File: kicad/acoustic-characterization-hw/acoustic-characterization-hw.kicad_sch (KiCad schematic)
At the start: 0 parts

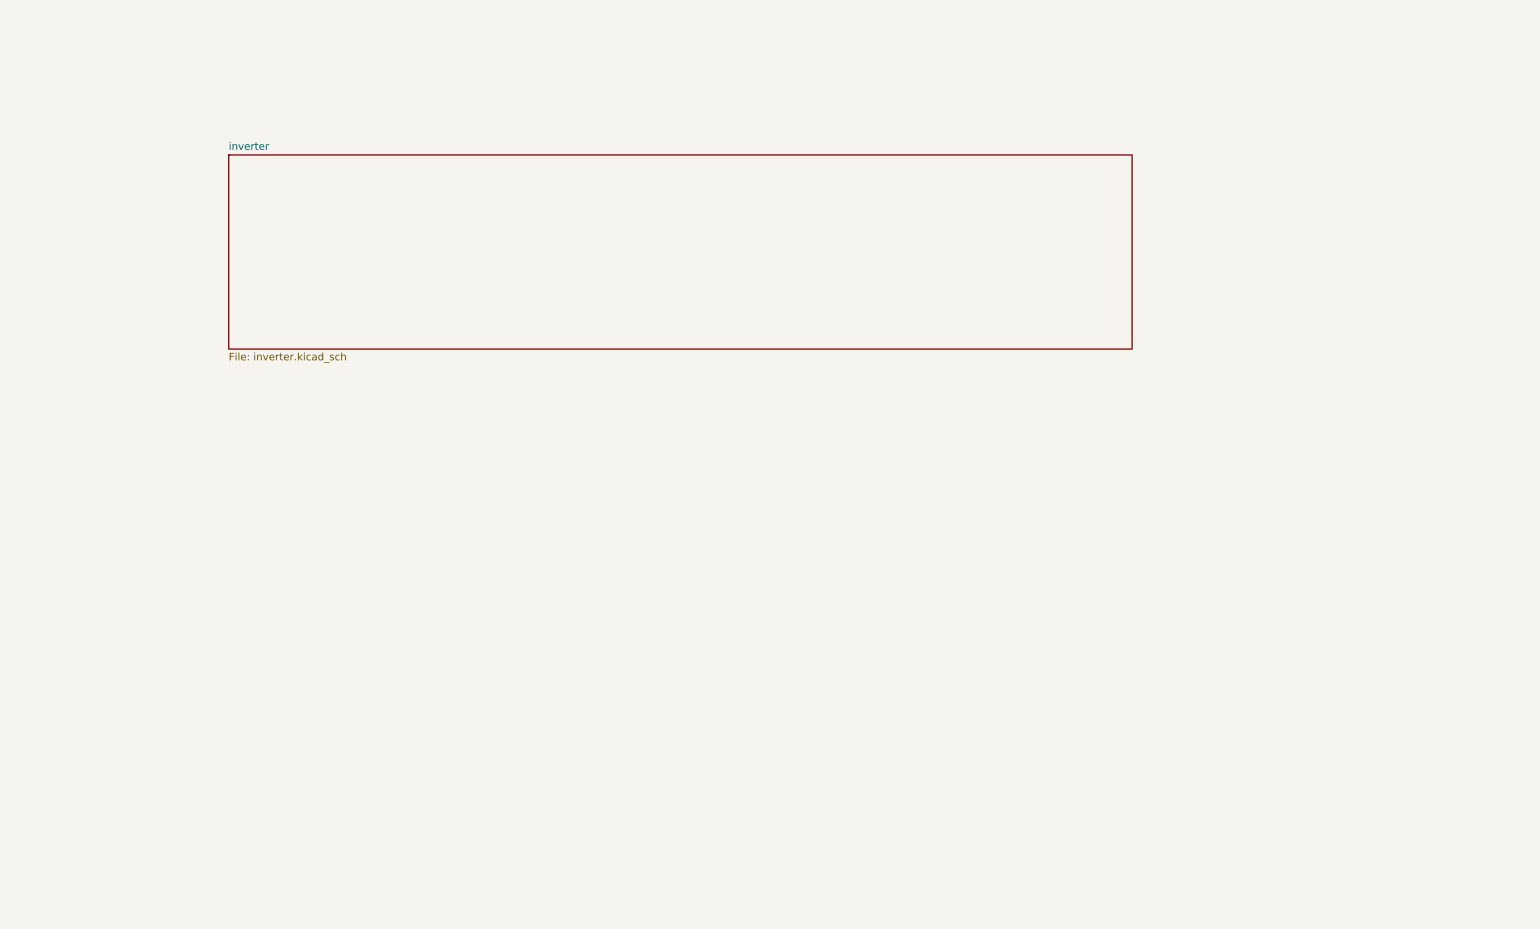
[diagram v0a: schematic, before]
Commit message: [kicad] Added analog front-end schematic and MS9280 symbol
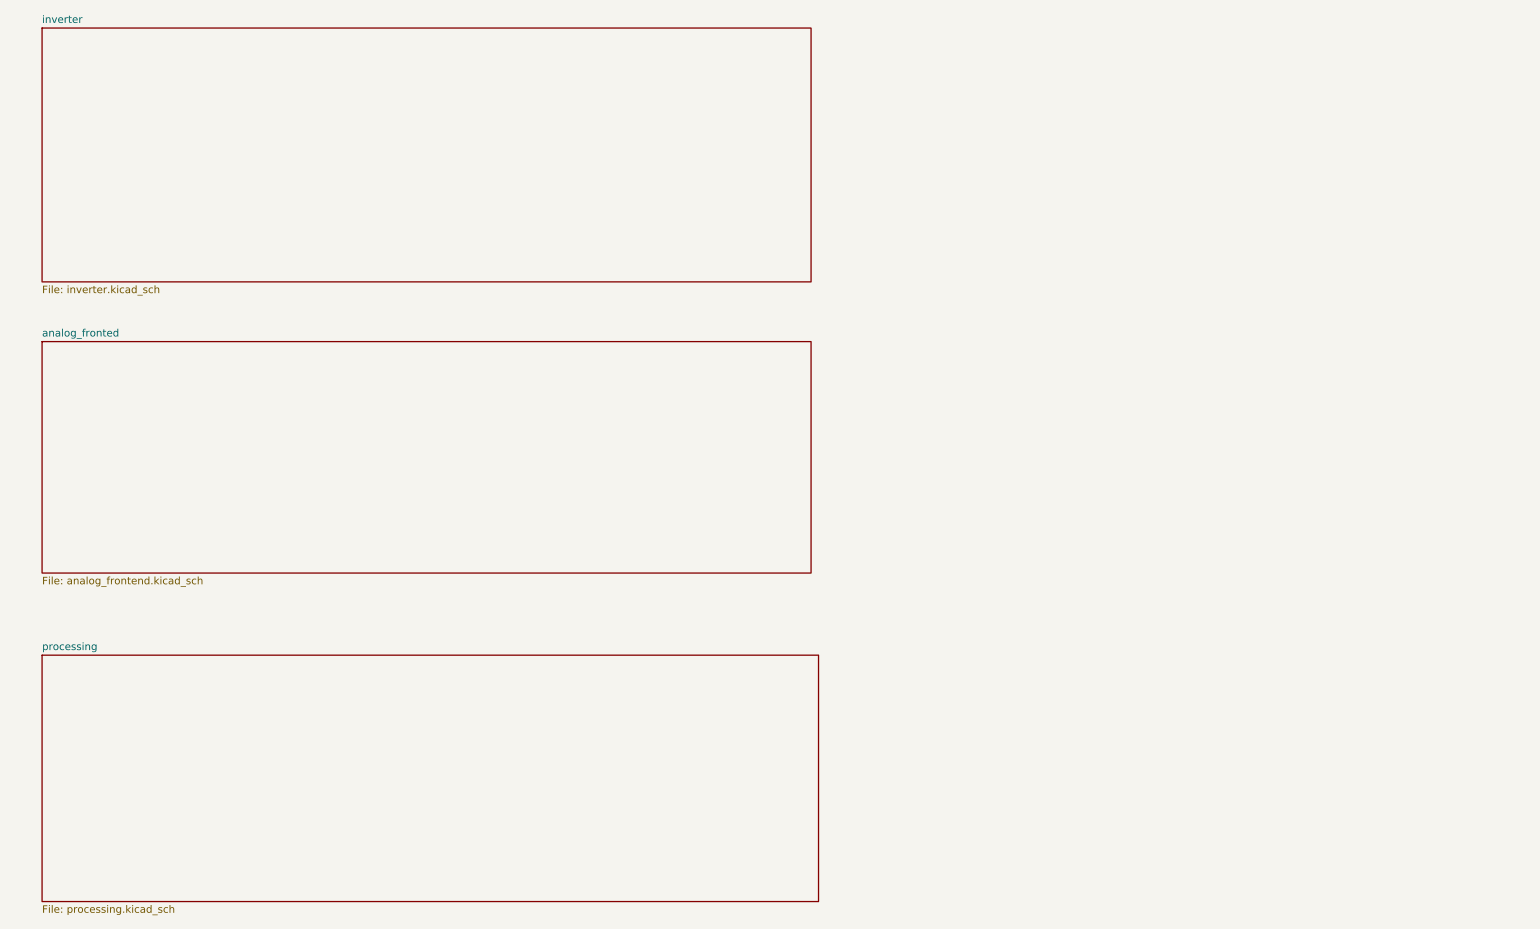
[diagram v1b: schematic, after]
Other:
- added sheet analog_fronted (analog_frontend.kicad_sch)
- added sheet processing (processing.kicad_sch)
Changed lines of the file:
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@@
 	(paper "A4")
 	(sheet
-		(at 52.07 43.18)
-		(size 153.67 33.02)
+		(at 20.32 74.93)
+		(size 130.81 39.37)
+		(fields_autoplaced yes)
+		(stroke
+			(width 0.1524)
+			(type solid)
+		)
+		(fill
+			(color 0 0 0 0.0000)
+		)
+		(property "Sheetname" "analog_fronted"
+			(at 20.32 74.2184 0)
+			(effects
+				(font
+					(size 1.27 1.27)
+				)
+				(justify left bottom)
+			)
+		)
+		(property "Sheetfile" "analog_frontend.kicad_sch"
+			(at 20.32 114.8846 0)
+			(effects
+				(font
+					(size 1.27 1.27)
+				)
+				(justify left top)
+			)
+		)
+		(instances
+			(project "acoustic-characterization-hw"
+				(path "/25b015c9-ab13-4427-b72c-b6f348597100"
+					(page "3")
+				)
+			)
+		)
+	)
+	(sheet
+		(at 20.32 128.27)
+		(size 132.08 41.91)
+		(fields_autoplaced yes)
+		(stroke
+			(width 0.1524)
+			(type solid)
+		)
+		(fill
+			(color 0 0 0 0.0000)
+		)
+		(property "Sheetname" "processing"
+			(at 20.32 127.5584 0)
+			(effects
+				(font
+					(size 1.27 1.27)
+				)
+				(justify left bottom)
+			)
+		)
+		(property "Sheetfile" "processing.kicad_sch"
+			(at 20.32 170.7646 0)
+			(effects
+				(font
+					(size 1.27 1.27)
+				)
+				(justify left top)
+			)
+		)
+		(instances
+			(project "acoustic-characterization-hw"
+				(path "/25b015c9-ab13-4427-b72c-b6f348597100"
+					(page "4")
+				)
+			)
+		)
+	)
+	(sheet
+		(at 20.32 21.59)
+		(size 130.81 43.18)
 		(fields_autoplaced yes)
 		(stroke
@@
 		)
 		(property "Sheetname" "inverter"
-			(at 52.07 42.4684 0)
+			(at 20.32 20.8784 0)
 			(effects
 				(font
@@
 		)
 		(property "Sheetfile" "inverter.kicad_sch"
-			(at 52.07 76.7846 0)
+			(at 20.32 65.3546 0)
 			(effects
 				(font

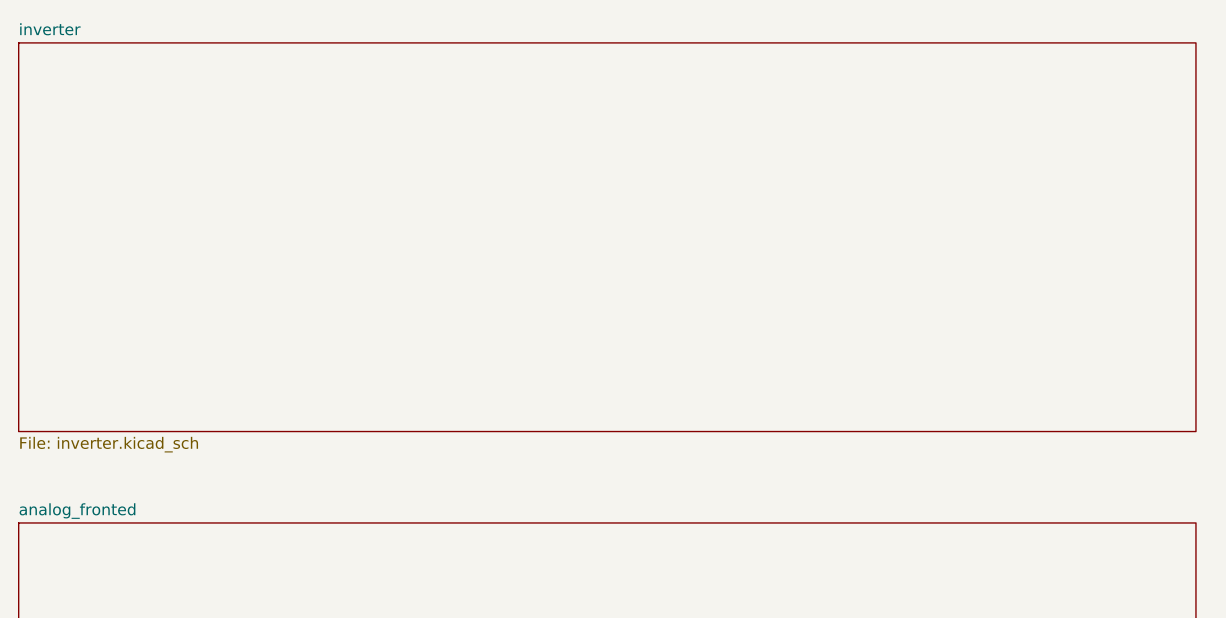
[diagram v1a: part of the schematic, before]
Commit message: [kicad, documentation] Set pin configuration, kept possibility open for reference voltage change and top/bottom, center, differential mode
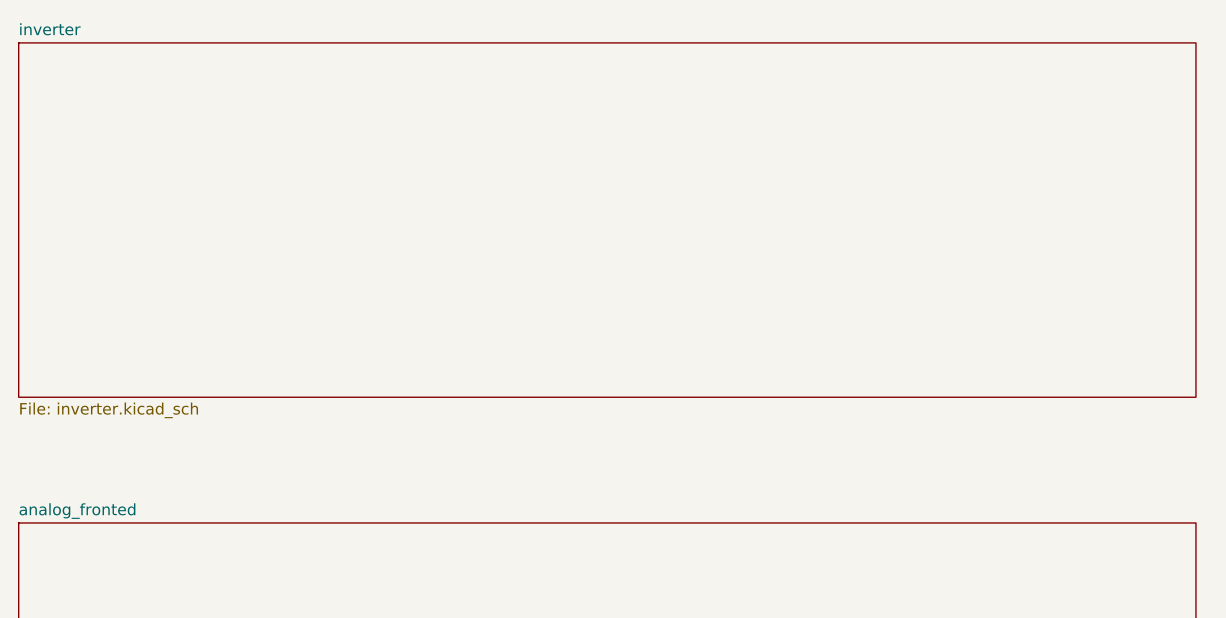
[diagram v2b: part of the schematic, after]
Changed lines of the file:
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@@
 	(sheet
 		(at 20.32 21.59)
-		(size 130.81 43.18)
+		(size 130.81 39.37)
 		(fields_autoplaced yes)
 		(stroke
@@
 		)
 		(property "Sheetfile" "inverter.kicad_sch"
-			(at 20.32 65.3546 0)
+			(at 20.32 61.5446 0)
 			(effects
 				(font

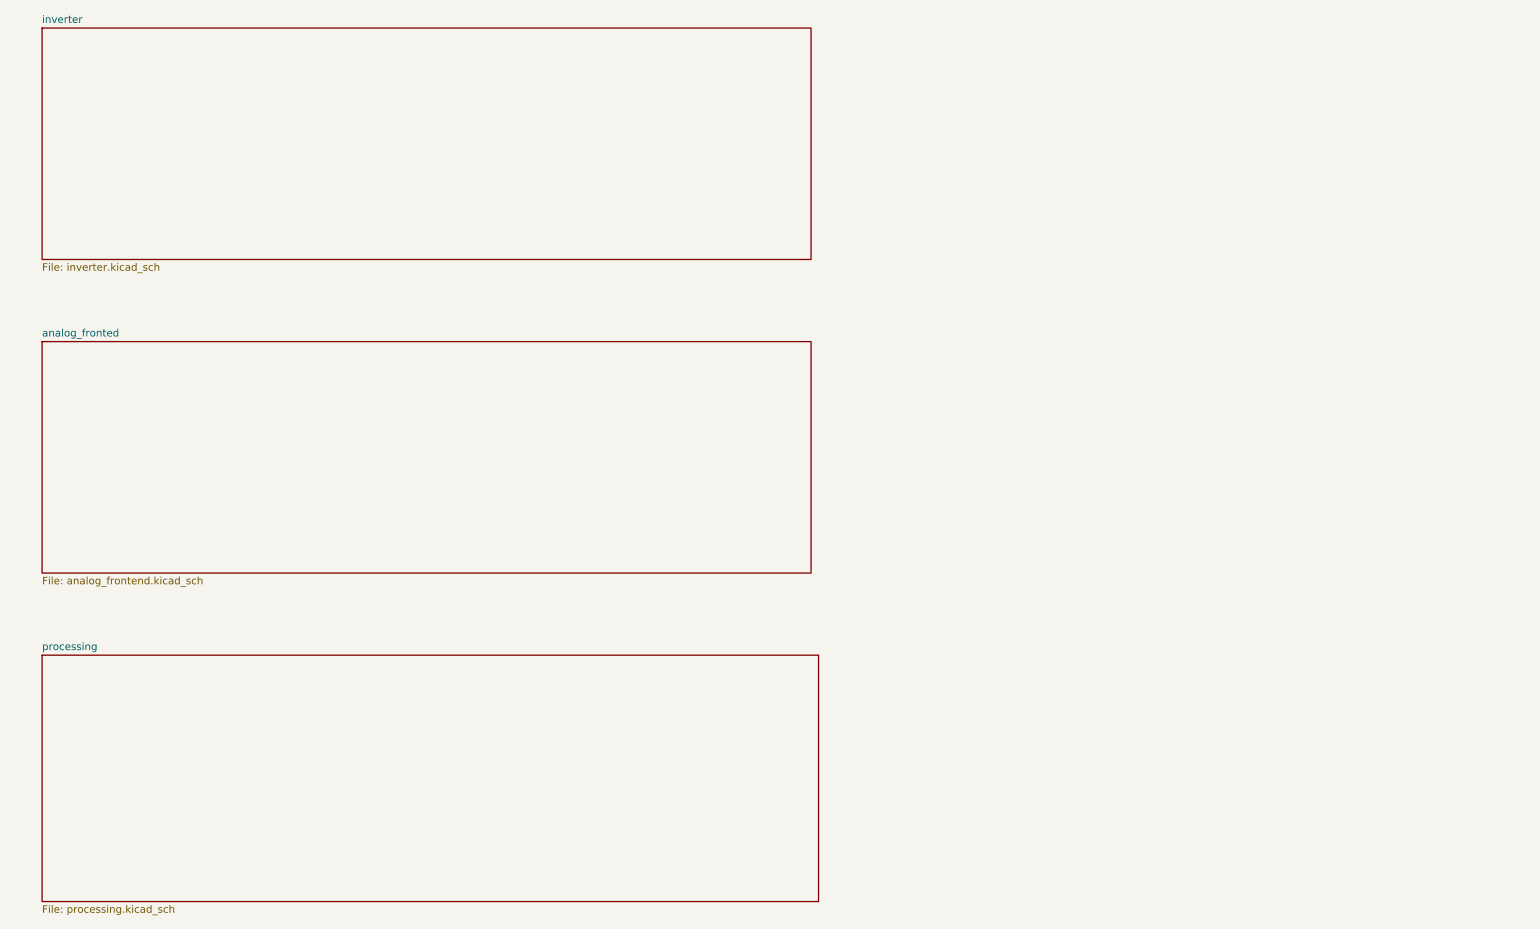
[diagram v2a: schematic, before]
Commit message: [kicad] Added initial config and jtag circuitrtry, added kicad symbol, added pinout + script for functionality checking (next) add qspi flash for boot
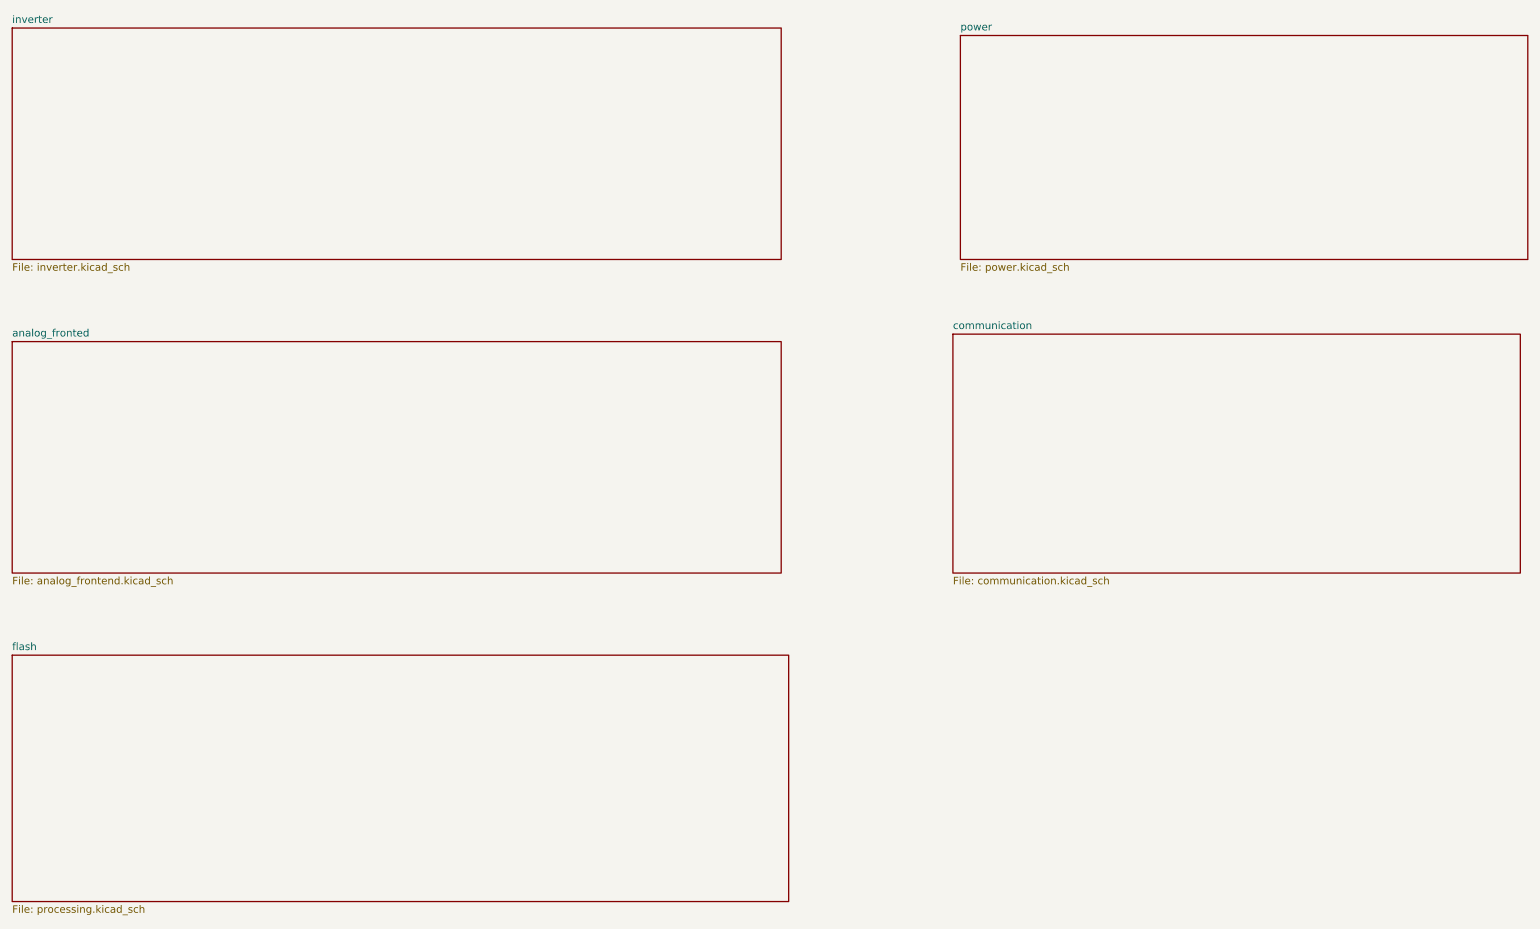
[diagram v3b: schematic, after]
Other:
- sheet processing renamed flash
- added sheet communication (communication.kicad_sch)
- added sheet power (power.kicad_sch)
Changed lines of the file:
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@@
 (kicad_sch
-	(version 20231120)
+	(version 20250114)
 	(generator "eeschema")
-	(generator_version "8.0")
+	(generator_version "9.0")
 	(paper "A4")
 	(sheet
-		(at 20.32 74.93)
+		(at 15.24 74.93)
 		(size 130.81 39.37)
+		(exclude_from_sim no)
+		(in_bom yes)
+		(on_board yes)
+		(dnp no)
 		(fields_autoplaced yes)
 		(stroke
@@
 		)
 		(property "Sheetname" "analog_fronted"
-			(at 20.32 74.2184 0)
+			(at 15.24 74.2184 0)
 			(effects
 				(font
@@
 		)
 		(property "Sheetfile" "analog_frontend.kicad_sch"
-			(at 20.32 114.8846 0)
+			(at 15.24 114.8846 0)
 			(effects
 				(font
@@
 	)
 	(sheet
-		(at 20.32 128.27)
+		(at 15.24 128.27)
 		(size 132.08 41.91)
-		(fields_autoplaced yes)
-		(stroke
-			(width 0.1524)
-			(type solid)
-		)
-		(fill
-			(color 0 0 0 0.0000)
-		)
-		(property "Sheetname" "processing"
-			(at 20.32 127.5584 0)
+		(exclude_from_sim no)
+		(in_bom yes)
+		(on_board yes)
+		(dnp no)
+		(fields_autoplaced yes)
+		(stroke
+			(width 0.1524)
+			(type solid)
+		)
+		(fill
+			(color 0 0 0 0.0000)
+		)
+		(property "Sheetname" "flash"
+			(at 15.24 127.5584 0)
 			(effects
 				(font
@@
 		)
 		(property "Sheetfile" "processing.kicad_sch"
-			(at 20.32 170.7646 0)
+			(at 15.24 170.7646 0)
 			(effects
 				(font
@@
 	)
 	(sheet
-		(at 20.32 21.59)
+		(at 15.24 21.59)
 		(size 130.81 39.37)
+		(exclude_from_sim no)
+		(in_bom yes)
+		(on_board yes)
+		(dnp no)
 		(fields_autoplaced yes)
 		(stroke
@@
 		)
 		(property "Sheetname" "inverter"
-			(at 20.32 20.8784 0)
+			(at 15.24 20.8784 0)
 			(effects
 				(font
@@
 		)
 		(property "Sheetfile" "inverter.kicad_sch"
-			(at 20.32 61.5446 0)
+			(at 15.24 61.5446 0)
 			(effects
 				(font
@@
 				(path "/25b015c9-ab13-4427-b72c-b6f348597100"
 					(page "2")
+				)
+			)
+		)
+	)
+	(sheet
+		(at 176.53 22.86)
+		(size 96.52 38.1)
+		(exclude_from_sim no)
+		(in_bom yes)
+		(on_board yes)
+		(dnp no)
+		(fields_autoplaced yes)
+		(stroke
+			(width 0.1524)
+			(type solid)
+		)
+		(fill
+			(color 0 0 0 0.0000)
+		)
+		(property "Sheetname" "power"
+			(at 176.53 22.1484 0)
+			(effects
+				(font
+					(size 1.27 1.27)
+				)
+				(justify left bottom)
+			)
+		)
+		(property "Sheetfile" "power.kicad_sch"
+			(at 176.53 61.5446 0)
+			(effects
+				(font
+					(size 1.27 1.27)
+				)
+				(justify left top)
+			)
+		)
+		(property "Field2" ""
+			(at 176.53 22.86 0)
+			(effects
+				(font
+					(size 1.27 1.27)
+				)
+			)
+		)
+		(instances
+			(project "acoustic-characterization-hw"
+				(path "/25b015c9-ab13-4427-b72c-b6f348597100"
+					(page "5")
+				)
+			)
+		)
+	)
+	(sheet
+		(at 175.26 73.66)
+		(size 96.52 40.64)
+		(exclude_from_sim no)
+		(in_bom yes)
+		(on_board yes)
+		(dnp no)
+		(fields_autoplaced yes)
+		(stroke
+			(width 0.1524)
+			(type solid)
+		)
+		(fill
+			(color 0 0 0 0.0000)
+		)
+		(property "Sheetname" "communication"
+			(at 175.26 72.9484 0)
+			(effects
+				(font
+					(size 1.27 1.27)
+				)
+				(justify left bottom)
+			)
+		)
+		(property "Sheetfile" "communication.kicad_sch"
+			(at 175.26 114.8846 0)
+			(effects
+				(font
+					(size 1.27 1.27)
+				)
+				(justify left top)
+			)
+		)
+		(property "Field2" ""
+			(at 175.26 73.66 0)
+			(effects
+				(font
+					(size 1.27 1.27)
+				)
+			)
+		)
+		(instances
+			(project "acoustic-characterization-hw"
+				(path "/25b015c9-ab13-4427-b72c-b6f348597100"
+					(page "6")
 				)
 			)
@@
 		)
 	)
+	(embedded_fonts no)
 )
